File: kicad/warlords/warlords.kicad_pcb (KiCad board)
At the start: 2 copper layers, 300 x 300 mm, 12 parts

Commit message: Draw every device at its real package size
The board maps existed to answer "which chip is at C4", and then drew a
24-pin ROM and a 20-pin LS245 as the same 14-pin outline. package_for()
read pin counts from DEVICES, which holds 20 Pong-era parts against the
112 part types the boards actually use, and silently fell back to DIP-14
for the other 92.

tools/packages.py is the pin-count table, kept separate from devices.py
on purpose: packaging needs one number for every part on every board,
while devices.py carries verified pinouts for the parts validate_nets.py
reasons about, and widening that set to satisfy a drawing would let the
extractor trust readings nothing has checked.

688 of 704 devices now size. check_packages.py re-derives 56 of the
entries from KiCAD's symbol library — comparing the highest pin number,
not the pin count, since KiCAD omits no-connects and a 7493 symbol has
ten pins on a DIP-14 — and confirms all 20 parts in DEVICES agree. The
Am2901 slices and the POKEY come from DIP-40 stated on the Battlezone
sheet; the 8316E from the drawing's note that a 2708 may be fitted
instead.

What does not size is now said out loud rather than quietly drawn at 14
pins: four descriptions recorded where the sheet gave no part number,
and the Atari 0351xx ROM/PROM numbers, which get the class default and
are listed as unverified until someone has a board in front of them.

Two things found while reading the corpus for packages, both logged in
asteroids.read.json rather than acted on. The -06 rate multiplier
resolution was recorded and never applied to the board data, and the
parts list disagrees with both readings on designators. F4/H4/J4 take
either an LS670 or an LS170, and the 19-007 pull-up network is fitted
only with the LS170 — same package either way, but a real failure mode.

Also: republishing a board without --machine used to unlink it from its
machine, because most definitions carry no machine of their own and the
link lived only in boards.json. publish_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
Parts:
- UL6, UM6, UN5, UN6, UP4, UP5, UP6: footprint DIP-14_W7.62mm -> DIP-16_W7.62mm

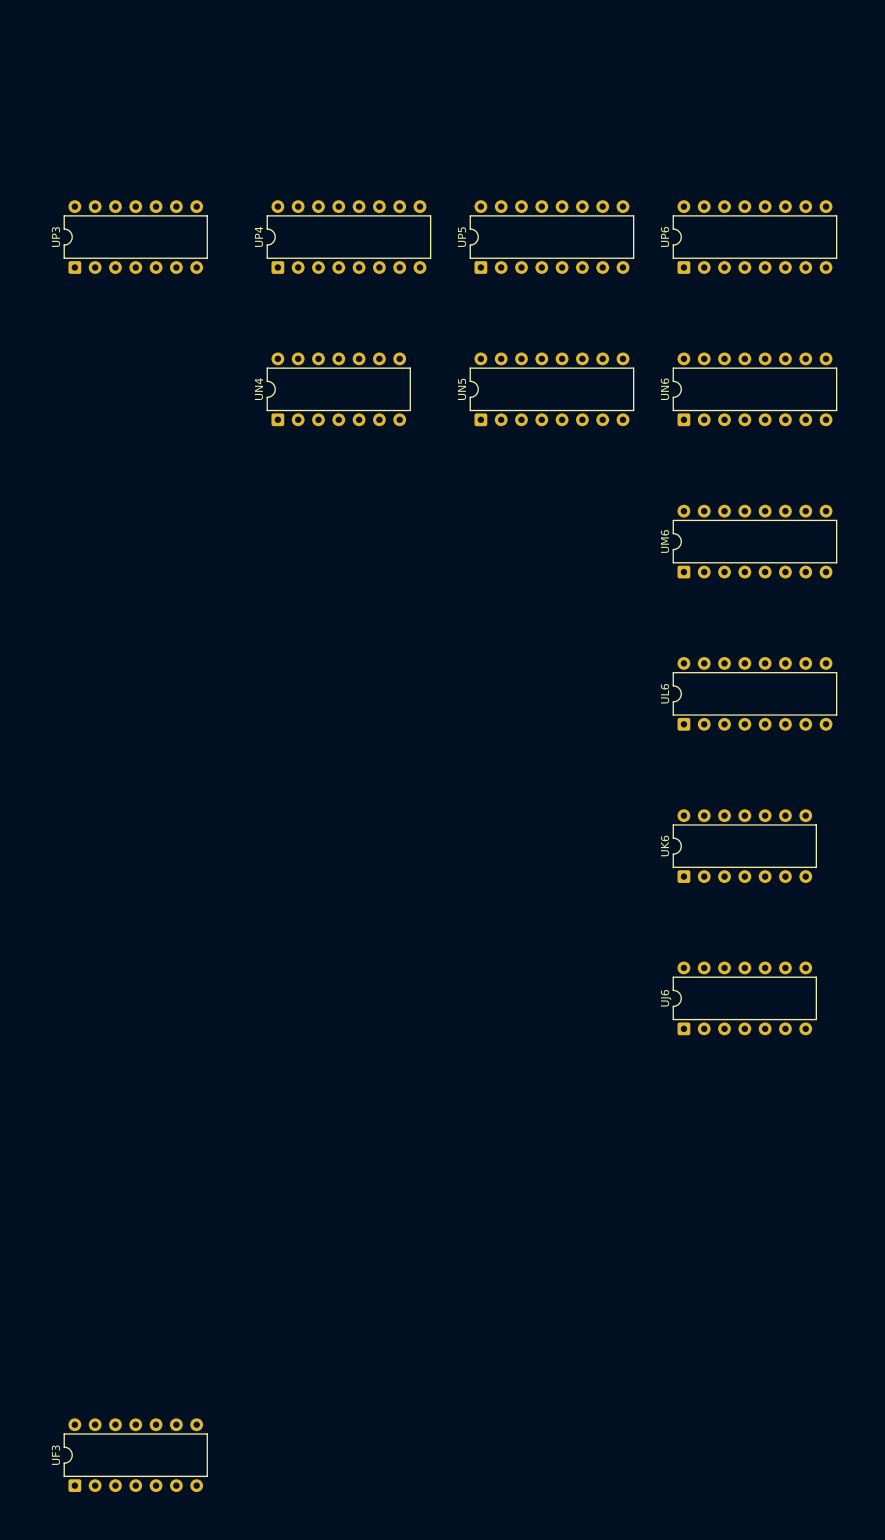
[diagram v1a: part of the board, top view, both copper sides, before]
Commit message: Drop two grid rows that do not exist, and span the devices that do
Atari's grid alphabet skips G, I, O and Q, and the board definitions
listed G and Q as rows. Every device below F was therefore drawn a row
too low, the rendered board carried two empty bands, and F/H1 looked
like a three-position span for a part 1.2in long on a 0.75in pitch.

Confirmed three ways before touching it. Nothing in any read, signature
or signal record in this repo sits in a G or Q row, while both
neighbours of each are populated on the two densest boards — Battlezone
P:6 R:2, Asteroids-03 P:4 R:3. The sheets' own spanning designators
treat F and H as adjacent and H and J as adjacent, which is only
possible if G and I are not positions. And with G removed, F/H falls out
as an adjacent pair, which is what a 24-pin ROM needs. Pong predates the
convention and legitimately uses G, so it keeps its grid.

Spans are now data rather than prose. A device drawn across two or three
cells is still keyed at its first cell, because that is the only thing
`ics` may be keyed by, but the sheet's own designator goes in a `spans`
map and the footprint is placed at the mean of the cells it names. A
DIP-40 at B/C2 sits between B2 and C2 instead of hanging equally over A2
and C2. The build rejects a span whose rows are not adjacent — that
failure almost always means the grid is wrong, not the span.

Two more inconsistencies found and logged rather than guessed at. Two of
the Math Box's four Am2901 slices carry a span and two do not, though
all four are the same DIP-40 on the same pitch. And asteroids-04.json
carries five devices at the -03 PROM positions alongside the -04 ROMs
and is missing 035144-02 at D/E1, contradicting the substitution table,
memory_by_revision and its own status text in the same breath.

Co-Authored-By: Claude Opus 5 <noreply@anthropic.com>
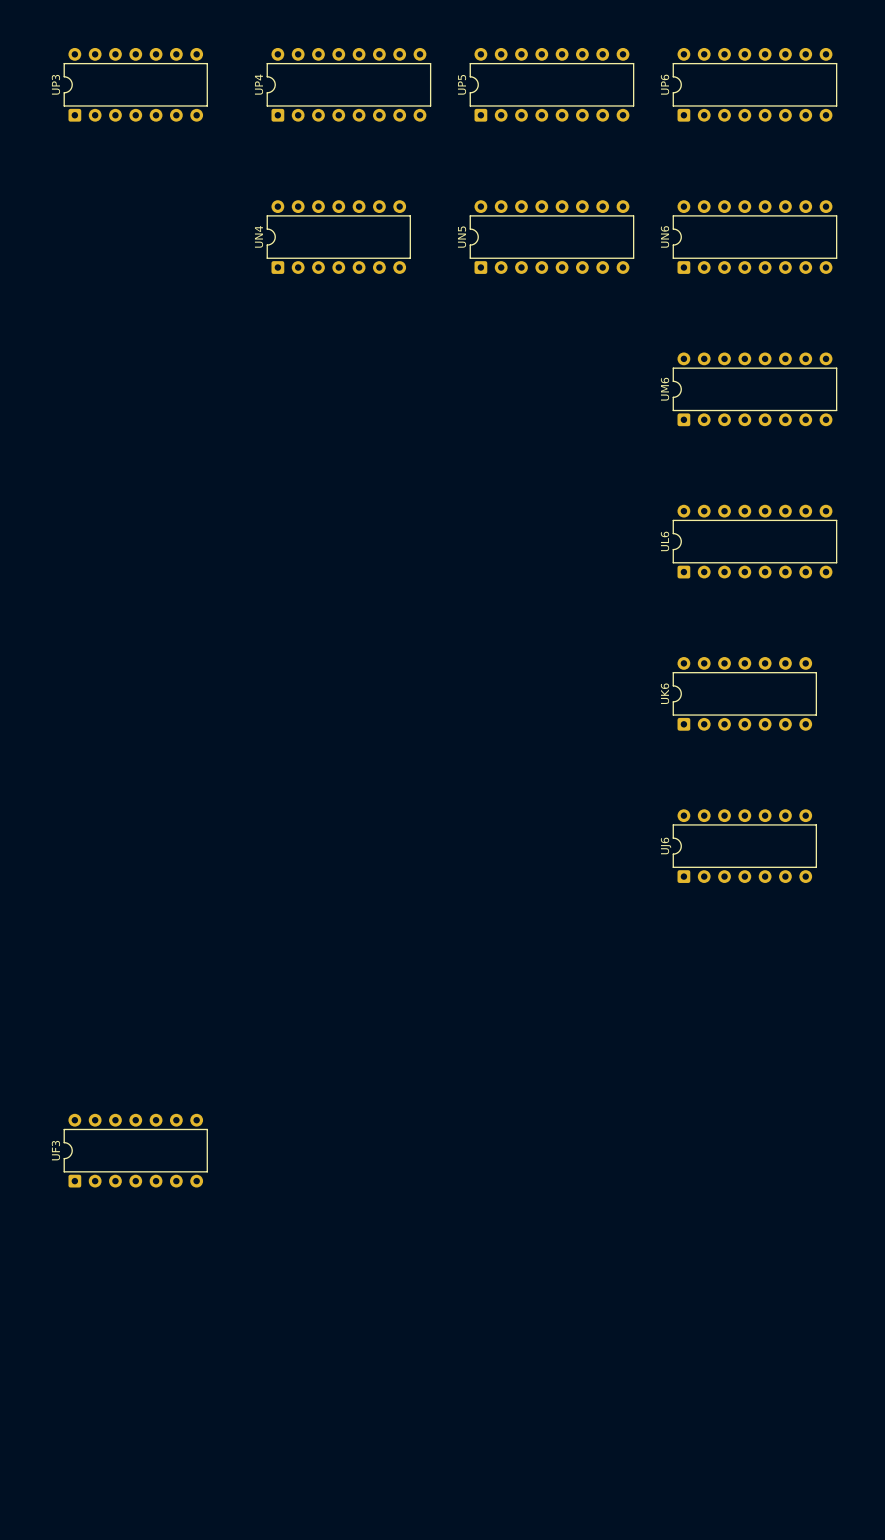
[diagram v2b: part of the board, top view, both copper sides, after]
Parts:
- moved UF3 38.1 mm to (76.8, 170.4)
- moved UK6 19.1 mm to (153.0, 113.2)
- moved UN4 19.1 mm to (102.2, 56.1)
- moved UN5 19.1 mm to (127.6, 56.1)
- moved UN6 19.1 mm to (153.0, 56.1)
- moved UP3 19.1 mm to (76.8, 37.0)
- moved UP4 19.1 mm to (102.2, 37.0)
- moved UP5 19.1 mm to (127.6, 37.0)
- moved UP6 19.1 mm to (153.0, 37.0)
- moved UL6 19.0 mm to (153.0, 94.2)
- moved UM6 19.0 mm to (153.0, 75.2)
- moved UJ6 19.0 mm to (153.0, 132.3)
